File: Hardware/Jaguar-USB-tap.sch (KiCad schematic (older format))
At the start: 24 parts, among them J1 DB15, P1 CONN_01X03, P2 USB_B, P3 CONN_01X05, U1 NCP1117ST33T3G, U2 STM32F070F6, U3 TXB0106, U4 TXB0106, Y1 8MHz

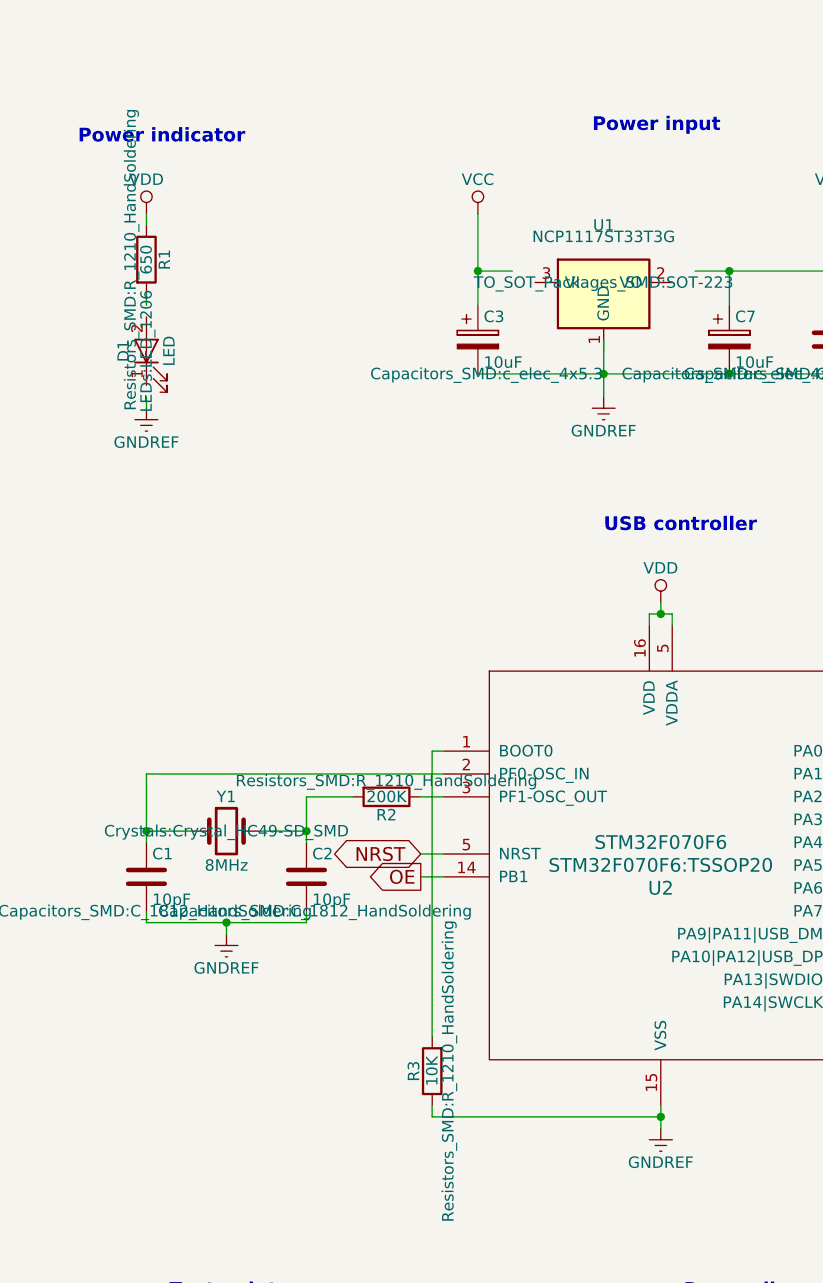
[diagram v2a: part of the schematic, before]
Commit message: Circuit improvements.
1) Add an indicator LED to OE.
2) Add a capacitor to NRST.
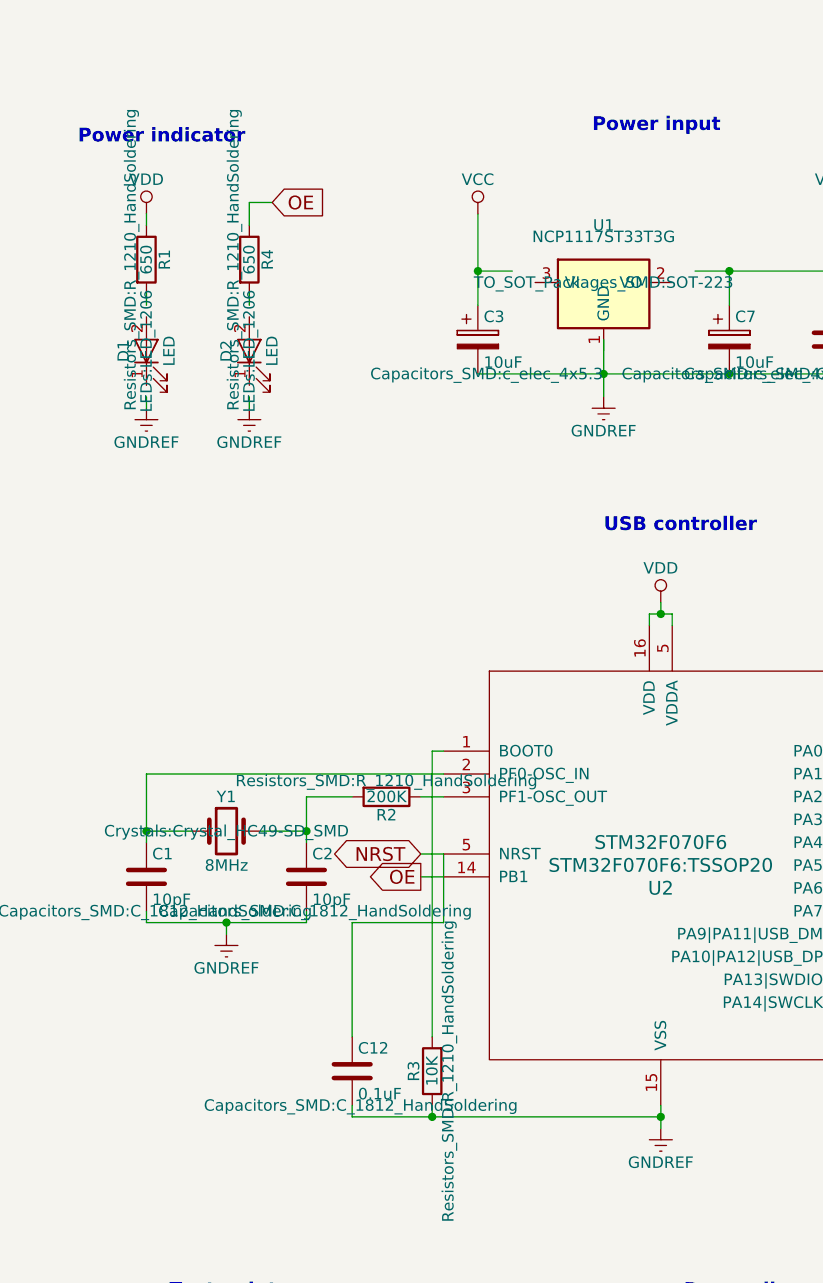
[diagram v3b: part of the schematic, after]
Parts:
- added C12: 0.1uF, Capacitors_SMD:C_1812_HandSoldering, symbol C
- added D2: LED, LEDs:LED_1206, symbol LED
- added R4: 650, Resistors_SMD:R_1210_HandSoldering, symbol R
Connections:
- wire segments 136 -> 144
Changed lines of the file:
@@
 $EndComp
 $Comp
-L GNDREF #PWR10
+L GNDREF #PWR01
 U 1 1 5A12FF66
 P 3500 5800
-F 0 "#PWR10" H 3500 5550 50  0001 C CNN
+F 0 "#PWR01" H 3500 5550 50  0001 C CNN
 F 1 "GNDREF" H 3500 5650 50  0000 C CNN
 F 2 "" H 3500 5800 50  0000 C CNN
@@
 $EndComp
 $Comp
-L VDD #PWR9
+L VDD #PWR02
 U 1 1 5A12FF9A
 P 3500 3500
-F 0 "#PWR9" H 3500 3350 50  0001 C CNN
+F 0 "#PWR02" H 3500 3350 50  0001 C CNN
 F 1 "VDD" H 3500 3650 50  0000 C CNN
 F 2 "" H 3500 3500 50  0000 C CNN
@@
 $EndComp
 $Comp
-L GNDREF #PWR2
+L GNDREF #PWR03
 U 1 1 5A1303C8
 P 1250 2650
-F 0 "#PWR2" H 1250 2400 50  0001 C CNN
+F 0 "#PWR03" H 1250 2400 50  0001 C CNN
 F 1 "GNDREF" H 1250 2500 50  0000 C CNN
 F 2 "" H 1250 2650 50  0000 C CNN
@@
 $EndComp
 $Comp
-L VDD #PWR1
+L VDD #PWR04
 U 1 1 5A130400
 P 1250 1800
-F 0 "#PWR1" H 1250 1650 50  0001 C CNN
+F 0 "#PWR04" H 1250 1650 50  0001 C CNN
 F 1 "VDD" H 1250 1950 50  0000 C CNN
 F 2 "" H 1250 1800 50  0000 C CNN
@@
 D-
 $Comp
-L GNDREF #PWR23
+L GNDREF #PWR05
 U 1 1 5A130C9B
 P 9500 2050
-F 0 "#PWR23" H 9500 1800 50  0001 C CNN
+F 0 "#PWR05" H 9500 1800 50  0001 C CNN
 F 1 "GNDREF" H 9500 1900 50  0000 C CNN
 F 2 "" H 9500 2050 50  0000 C CNN
@@
 $EndComp
 $Comp
-L VCC #PWR22
+L VCC #PWR06
 U 1 1 5A130DFE
 P 9500 1400
-F 0 "#PWR22" H 9500 1250 50  0001 C CNN
+F 0 "#PWR06" H 9500 1250 50  0001 C CNN
 F 1 "VCC" H 9500 1550 50  0000 C CNN
 F 2 "" H 9500 1400 50  0000 C CNN
@@
 SWCLK
 $Comp
-L VDD #PWR26
+L VDD #PWR07
 U 1 1 5A13106E
 P 9550 5500
-F 0 "#PWR26" H 9550 5350 50  0001 C CNN
+F 0 "#PWR07" H 9550 5350 50  0001 C CNN
 F 1 "VDD" H 9550 5650 50  0000 C CNN
 F 2 "" H 9550 5500 50  0000 C CNN
@@
 $EndComp
 $Comp
-L GNDREF #PWR27
+L GNDREF #PWR08
 U 1 1 5A13108E
 P 9550 6200
-F 0 "#PWR27" H 9550 5950 50  0001 C CNN
+F 0 "#PWR08" H 9550 5950 50  0001 C CNN
 F 1 "GNDREF" H 9550 6050 50  0000 C CNN
 F 2 "" H 9550 6200 50  0000 C CNN
@@
 $EndComp
 $Comp
-L GNDREF #PWR8
+L GNDREF #PWR09
 U 1 1 5A1314CC
 P 3250 2600
-F 0 "#PWR8" H 3250 2350 50  0001 C CNN
+F 0 "#PWR09" H 3250 2350 50  0001 C CNN
 F 1 "GNDREF" H 3250 2450 50  0000 C CNN
 F 2 "" H 3250 2600 50  0000 C CNN
@@
 $EndComp
 $Comp
-L VCC #PWR7
+L VCC #PWR010
 U 1 1 5A1317D5
 P 2700 1800
-F 0 "#PWR7" H 2700 1650 50  0001 C CNN
+F 0 "#PWR010" H 2700 1650 50  0001 C CNN
 F 1 "VCC" H 2700 1950 50  0000 C CNN
 F 2 "" H 2700 1800 50  0000 C CNN
@@
 $EndComp
 $Comp
-L VDD #PWR13
+L VDD #PWR011
 U 1 1 5A131C2A
 P 4250 1800
-F 0 "#PWR13" H 4250 1650 50  0001 C CNN
+F 0 "#PWR011" H 4250 1650 50  0001 C CNN
 F 1 "VDD" H 4250 1950 50  0000 C CNN
 F 2 "" H 4250 1800 50  0000 C CNN
@@
 $EndComp
 $Comp
-L GNDREF #PWR12
+L GNDREF #PWR012
 U 1 1 5A133640
 P 3500 7350
-F 0 "#PWR12" H 3500 7100 50  0001 C CNN
+F 0 "#PWR012" H 3500 7100 50  0001 C CNN
 F 1 "GNDREF" H 3500 7200 50  0000 C CNN
 F 2 "" H 3500 7350 50  0000 C CNN
@@
 $EndComp
 $Comp
-L VDD #PWR11
+L VDD #PWR013
 U 1 1 5A13366C
 P 3500 6850
-F 0 "#PWR11" H 3500 6700 50  0001 C CNN
+F 0 "#PWR013" H 3500 6700 50  0001 C CNN
 F 1 "VDD" H 3500 7000 50  0000 C CNN
 F 2 "" H 3500 6850 50  0000 C CNN
@@
 $EndComp
 $Comp
-L GNDREF #PWR4
+L GNDREF #PWR014
 U 1 1 5A134BEB
 P 1600 4950
-F 0 "#PWR4" H 1600 4700 50  0001 C CNN
+F 0 "#PWR014" H 1600 4700 50  0001 C CNN
 F 1 "GNDREF" H 1600 4800 50  0000 C CNN
 F 2 "" H 1600 4950 50  0000 C CNN
@@
 $EndComp
 $Comp
-L VDD #PWR16
+L VDD #PWR015
 U 1 1 5A135B5A
 P 6800 1750
-F 0 "#PWR16" H 6800 1600 50  0001 C CNN
+F 0 "#PWR015" H 6800 1600 50  0001 C CNN
 F 1 "VDD" H 6800 1900 50  0000 C CNN
 F 2 "" H 6800 1750 50  0000 C CNN
@@
 $EndComp
 $Comp
-L VDD #PWR17
+L VDD #PWR016
 U 1 1 5A135B94
 P 6800 3700
-F 0 "#PWR17" H 6800 3550 50  0001 C CNN
+F 0 "#PWR016" H 6800 3550 50  0001 C CNN
 F 1 "VDD" H 6800 3850 50  0000 C CNN
 F 2 "" H 6800 3700 50  0000 C CNN
@@
 $EndComp
 $Comp
-L VCC #PWR20
+L VCC #PWR017
 U 1 1 5A135DA6
 P 8250 1750
-F 0 "#PWR20" H 8250 1600 50  0001 C CNN
+F 0 "#PWR017" H 8250 1600 50  0001 C CNN
 F 1 "VCC" H 8250 1900 50  0000 C CNN
 F 2 "" H 8250 1750 50  0000 C CNN
@@
 $EndComp
 $Comp
-L VCC #PWR21
+L VCC #PWR018
 U 1 1 5A135DE0
 P 8250 3700
-F 0 "#PWR21" H 8250 3550 50  0001 C CNN
+F 0 "#PWR018" H 8250 3550 50  0001 C CNN
 F 1 "VCC" H 8250 3850 50  0000 C CNN
 F 2 "" H 8250 3700 50  0000 C CNN
@@
 $EndComp
 $Comp
-L GNDREF #PWR18
+L GNDREF #PWR019
 U 1 1 5A136102
 P 7500 3150
-F 0 "#PWR18" H 7500 2900 50  0001 C CNN
+F 0 "#PWR019" H 7500 2900 50  0001 C CNN
 F 1 "GNDREF" H 7500 3000 50  0000 C CNN
 F 2 "" H 7500 3150 50  0000 C CNN
@@
 $EndComp
 $Comp
-L GNDREF #PWR19
+L GNDREF #PWR020
 U 1 1 5A13613C
 P 7500 5100
-F 0 "#PWR19" H 7500 4850 50  0001 C CNN
+F 0 "#PWR020" H 7500 4850 50  0001 C CNN
 F 1 "GNDREF" H 7500 4950 50  0000 C CNN
 F 2 "" H 7500 5100 50  0000 C CNN
@@
 $EndComp
 $Comp
-L GNDREF #PWR3
+L GNDREF #PWR021
 U 1 1 5A139451
 P 1250 7100
-F 0 "#PWR3" H 1250 6850 50  0001 C CNN
+F 0 "#PWR021" H 1250 6850 50  0001 C CNN
 F 1 "GNDREF" H 1250 6950 50  0000 C CNN
 F 2 "" H 1250 7100 50  0000 C CNN
@@
 $EndComp
 $Comp
-L VCC #PWR5
+L VCC #PWR022
 U 1 1 5A139495
 P 1750 6850
-F 0 "#PWR5" H 1750 6700 50  0001 C CNN
+F 0 "#PWR022" H 1750 6700 50  0001 C CNN
 F 1 "VCC" H 1700 7000 50  0000 C CNN
 F 2 "" H 1750 6850 50  0000 C CNN
@@
 $EndComp
 $Comp
-L VDD #PWR6
+L VDD #PWR023
 U 1 1 5A1394D9
 P 1850 6850
-F 0 "#PWR6" H 1850 6700 50  0001 C CNN
+F 0 "#PWR023" H 1850 6700 50  0001 C CNN
 F 1 "VDD" H 1900 7000 50  0000 C CNN
 F 2 "" H 1850 6850 50  0000 C CNN
@@
 Connection ~ 1600 4900
 Wire Wire Line
-	3500 5750 2500 5750
+	2150 5750 3500 5750
 Wire Wire Line
 	2500 5750 2500 5700
@@
 $EndComp
 $Comp
-L GNDREF #PWR15
+L GNDREF #PWR024
 U 1 1 5A13DB5E
 P 4650 7350
-F 0 "#PWR15" H 4650 7100 50  0001 C CNN
+F 0 "#PWR024" H 4650 7100 50  0001 C CNN
 F 1 "GNDREF" H 4650 7200 50  0000 C CNN
 F 2 "" H 4650 7350 50  0000 C CNN
@@
 $EndComp
 $Comp
-L VCC #PWR14
+L VCC #PWR025
 U 1 1 5A13DBA2
 P 4650 6850
-F 0 "#PWR14" H 4650 6700 50  0001 C CNN
+F 0 "#PWR025" H 4650 6700 50  0001 C CNN
 F 1 "VCC" H 4650 7000 50  0000 C CNN
 F 2 "" H 4650 6850 50  0000 C CNN
@@
 Connection ~ 4650 7300
 $Comp
-L VCC #PWR24
+L VCC #PWR026
 U 1 1 5A13E476
 P 9500 2950
-F 0 "#PWR24" H 9500 2800 50  0001 C CNN
+F 0 "#PWR026" H 9500 2800 50  0001 C CNN
 F 1 "VCC" H 9500 3100 50  0000 C CNN
 F 2 "" H 9500 2950 50  0000 C CNN
@@
 $EndComp
 $Comp
-L GNDREF #PWR25
+L GNDREF #PWR027
 U 1 1 5A13E534
 P 9500 4750
-F 0 "#PWR25" H 9500 4500 50  0001 C CNN
+F 0 "#PWR027" H 9500 4500 50  0001 C CNN
 F 1 "GNDREF" H 9500 4600 50  0000 C CNN
 F 2 "" H 9500 4750 50  0000 C CNN
@@
 	9350 3450 9650 3450
 $Comp
-L GNDREF #PWR?
+L GNDREF #PWR028
 U 1 1 5A144546
 P 4900 1500
-F 0 "#PWR?" H 4900 1250 50  0001 C CNN
+F 0 "#PWR028" H 4900 1250 50  0001 C CNN
 F 1 "GNDREF" H 4900 1350 50  0000 C CNN
 F 2 "" H 4900 1500 50  0000 C CNN
@@
 $EndComp
 $Comp
-L VCC #PWR?
+L VCC #PWR029
 U 1 1 5A14458A
 P 5250 1200
-F 0 "#PWR?" H 5250 1050 50  0001 C CNN
+F 0 "#PWR029" H 5250 1050 50  0001 C CNN
 F 1 "VCC" H 5250 1350 50  0000 C CNN
 F 2 "" H 5250 1200 50  0000 C CNN
@@
 $EndComp
 $Comp
-L VDD #PWR?
+L VDD #PWR030
 U 1 1 5A1445CE
 P 5550 1200
-F 0 "#PWR?" H 5550 1050 50  0001 C CNN
+F 0 "#PWR030" H 5550 1050 50  0001 C CNN
 F 1 "VDD" H 5550 1350 50  0000 C CNN
 F 2 "" H 5550 1200 50  0000 C CNN
@@
 $EndComp
 $Comp
-L PWR_FLAG #FLG?
+L PWR_FLAG #FLG031
 U 1 1 5A144612
 P 4900 1250
-F 0 "#FLG?" H 4900 1345 50  0001 C CNN
+F 0 "#FLG031" H 4900 1345 50  0001 C CNN
 F 1 "PWR_FLAG" H 4900 1430 50  0000 C CNN
 F 2 "" H 4900 1250 50  0000 C CNN
@@
 $EndComp
 $Comp
-L PWR_FLAG #FLG?
+L PWR_FLAG #FLG032
 U 1 1 5A1446FA
 P 5250 1500
-F 0 "#FLG?" H 5250 1595 50  0001 C CNN
+F 0 "#FLG032" H 5250 1595 50  0001 C CNN
 F 1 "PWR_FLAG" H 5250 1680 50  0000 C CNN
 F 2 "" H 5250 1500 50  0000 C CNN
@@
 $EndComp
 $Comp
-L PWR_FLAG #FLG?
+L PWR_FLAG #FLG033
 U 1 1 5A14473E
 P 5550 1500
-F 0 "#FLG?" H 5550 1595 50  0001 C CNN
+F 0 "#FLG033" H 5550 1595 50  0001 C CNN
 F 1 "PWR_FLAG" H 5550 1680 50  0000 C CNN
 F 2 "" H 5550 1500 50  0000 C CNN
@@
 Wire Wire Line
 	5550 1200 5550 1500
+$Comp
+L C C12
+U 1 1 5A146FC4
+P 2150 5550
+F 0 "C12" H 2175 5650 50  0000 L CNN
+F 1 "0.1uF" H 2175 5450 50  0000 L CNN
+F 2 "Capacitors_SMD:C_1812_HandSoldering" H 2188 5400 50  0000 C CNN
+F 3 "" H 2150 5550 50  0000 C CNN
+	1    2150 5550
+	1    0    0    -1
+$EndComp
+Wire Wire Line
+	2550 4600 2550 4900
+Wire Wire Line
+	2550 4900 2150 4900
+Wire Wire Line
+	2150 4900 2150 5400
+Wire Wire Line
+	2150 5700 2150 5750
+Connection ~ 2500 5750
+$Comp
+L LED D2
+U 1 1 5A1477B1
+P 1700 2400
+F 0 "D2" H 1700 2500 50  0000 C CNN
+F 1 "LED" H 1700 2300 50  0000 C CNN
+F 2 "LEDs:LED_1206" H 1700 2400 50  0000 C CNN
+F 3 "" H 1700 2400 50  0000 C CNN
+	1    1700 2400
+	0    -1   -1   0
+$EndComp
+$Comp
+L GNDREF #PWR034
+U 1 1 5A147824
+P 1700 2650
+F 0 "#PWR034" H 1700 2400 50  0001 C CNN
+F 1 "GNDREF" H 1700 2500 50  0000 C CNN
+F 2 "" H 1700 2650 50  0000 C CNN
+F 3 "" H 1700 2650 50  0000 C CNN
+	1    1700 2650
+	1    0    0    -1
+$EndComp
+$Comp
+L R R4
+U 1 1 5A14786C
+P 1700 2000
+F 0 "R4" V 1780 2000 50  0000 C CNN
+F 1 "650" V 1700 2000 50  0000 C CNN
+F 2 "Resistors_SMD:R_1210_HandSoldering" V 1630 2000 50  0000 C CNN
+F 3 "" H 1700 2000 50  0000 C CNN
+	1    1700 2000
+	1    0    0    -1
+$EndComp
+Text GLabel 1800 1750 2    60   Input ~ 0
+OE
+Wire Wire Line
+	1800 1750 1700 1750
+Wire Wire Line
+	1700 1750 1700 1850
+Wire Wire Line
+	1700 2150 1700 2200
+Wire Wire Line
+	1700 2600 1700 2650
 $EndSCHEMATC
